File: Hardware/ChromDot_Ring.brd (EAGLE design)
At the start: 27.9 x 27.9 mm, 23 parts, among them J1 APA102PAD, J2 APA102PAD

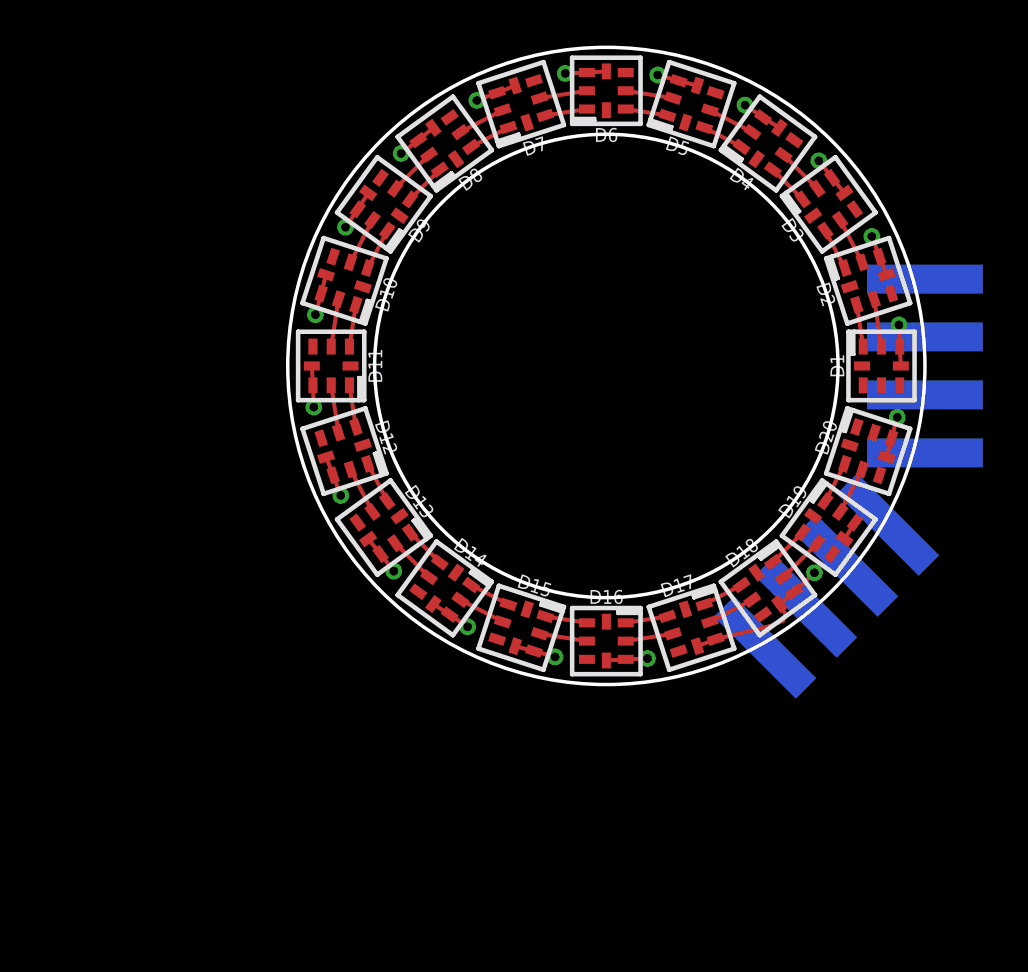
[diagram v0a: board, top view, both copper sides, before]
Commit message: adding apa102 rings
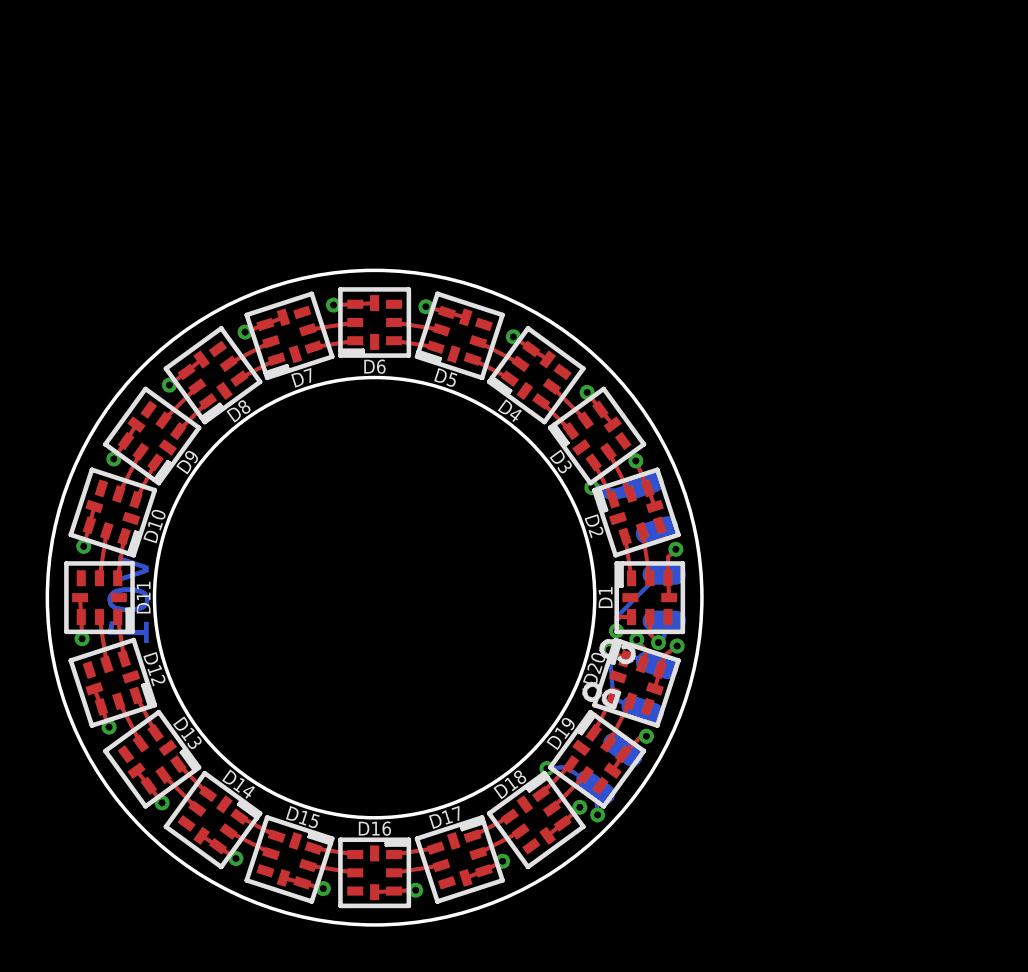
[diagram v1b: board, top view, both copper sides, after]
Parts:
- added J3, J4: DOUBLE_LED_PAD, Andy:DOUBLELEDPAD
- added U$1: (no value), buzzard_labels (22):CHROMADOT5
- added U$10: (no value), buzzard_labels (26):DI4
- added U$2: (no value), buzzard_labels (22):20_APA102_LED#S6
- added U$3, U$4: (no value), buzzard_labels (25):5V6
- added U$5, U$6: (no value), buzzard_labels (25):G4
- added U$7: (no value), buzzard_labels (25):DO3
- added U$8: (no value), buzzard_labels (25):CO1
- added U$9: (no value), buzzard_labels (26):CI6
- J1, J2: value APA102PAD -> DOUBLE_LED_PAD; device Andy:APA102PADS -> Andy:DOUBLELEDPAD
- moved D18 14.4 mm to (22.3, 5.49)
- moved D9 14.4 mm to (5.49, 22.3)
- moved D1 14.4 mm to (27.3, 15.2)
- moved D10 14.4 mm to (3.76, 19.0)
- moved D12 14.4 mm to (3.76, 11.5)
- moved D13 14.4 mm to (5.49, 8.15)
- moved D14 14.4 mm to (8.15, 5.49)
- moved D15 14.4 mm to (11.5, 3.76)
- moved D17 14.4 mm to (19.0, 3.76)
- moved D2 14.4 mm to (26.7, 19.0)
- moved D20 14.4 mm to (26.7, 11.5)
- moved D5 14.4 mm to (19.0, 26.7)
- moved D6 14.4 mm to (15.2, 27.3)
- moved D7 14.4 mm to (11.5, 26.7)
- moved D11 14.4 mm to (3.17, 15.2)
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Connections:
- net 5V: now also J1.P$2, J3.P$2; no longer J1.VDD, J2.VDD
- net GND: now also J1.P$1, J3.P$1; no longer J1.GND, J2.GND
- net N$2: now also J2.P$2; no longer J1.CLOCK
- net N$3: now also J2.P$1; no longer J1.DATA
- net N$41: now also J4.P$2; no longer J2.CLOCK
- net N$42: now also J4.P$1; no longer J2.DATA
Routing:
- net GND: track 0.00 -> 5.96 mm, vias 0 -> 3
- net N$3: track 0.00 -> 4.76 mm, vias 0 -> 1
- net N$42: track 0.00 -> 4.32 mm, vias 0 -> 1
- net N$41: track 0.00 -> 3.16 mm, vias 0 -> 1
- net N$2: track 0.00 -> 2.33 mm, vias 0 -> 1
- net 5V: track 38.4 -> 38.0 mm, vias 18 -> 20
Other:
- board size 27.9 x 27.9 mm -> 28.7 x 28.7 mm
- board text added: "v01"
